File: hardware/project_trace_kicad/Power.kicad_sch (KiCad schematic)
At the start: 12 parts, among them J501 FIT0587_Male, J502 FIT0587_Female, J503 Screw_Terminal_01x04, U501 UA78M33QDCYRQ1, U502 UA78M05QDCYRQ1

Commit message: ERC Checks & Bug-Fixing
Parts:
- renumbered A501 to A401, BT501 to BT401, BT502 to BT402, C503 to C401, C504 to C402, C401 to C403, C402 to C404, J501 to J401, J502 to J402, J503 to J403, U501 to U401, U502 to U402
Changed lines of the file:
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@@
 		(dnp no)
 		(fields_autoplaced yes)
-		(property "Reference" "#PWR0501"
+		(property "Reference" "#PWR0401"
 			(at 176.53 97.79 0)
 			(hide yes)
@@
 			(project "project_trace_kicad"
 				(path "/af51f4e5-b952-4b0e-baf2-78a72fb86fcd/12a73351-c59a-4c39-a723-2f90ff2520c9"
-					(reference "#PWR0501")
+					(reference "#PWR0401")
 					(unit 1)
 				)
@@
 		(in_pos_files yes)
 		(dnp no)
-		(property "Reference" "#FLG0502"
+		(property "Reference" "#FLG0402"
 			(at 167.64 93.345 0)
 			(hide yes)
@@
 			(project "project_trace_kicad"
 				(path "/af51f4e5-b952-4b0e-baf2-78a72fb86fcd/12a73351-c59a-4c39-a723-2f90ff2520c9"
-					(reference "#FLG0502")
+					(reference "#FLG0402")
 					(unit 1)
 				)
@@
 		(dnp no)
 		(fields_autoplaced yes)
-		(property "Reference" "C504"
+		(property "Reference" "C402"
 			(at 186.3091 117.4072 0)
 			(show_name no)
@@
 			(project "project_trace_kicad"
 				(path "/af51f4e5-b952-4b0e-baf2-78a72fb86fcd/12a73351-c59a-4c39-a723-2f90ff2520c9"
-					(reference "C504")
+					(reference "C402")
 					(unit 1)
 				)
@@
 		(dnp no)
 		(fields_autoplaced yes)
-		(property "Reference" "U501"
+		(property "Reference" "U401"
 			(at 198.12 80.9455 0)
 			(show_name no)
@@
 			(project "project_trace_kicad"
 				(path "/af51f4e5-b952-4b0e-baf2-78a72fb86fcd/12a73351-c59a-4c39-a723-2f90ff2520c9"
-					(reference "U501")
+					(reference "U401")
 					(unit 1)
 				)
@@
 		(dnp yes)
 		(fields_autoplaced yes)
-		(property "Reference" "J501"
+		(property "Reference" "J401"
 			(at 122.6312 100.3878 0)
 			(show_name no)
@@
 			(project "project_trace_kicad"
 				(path "/af51f4e5-b952-4b0e-baf2-78a72fb86fcd/12a73351-c59a-4c39-a723-2f90ff2520c9"
-					(reference "J501")
+					(reference "J401")
 					(unit 1)
 				)
@@
 		(dnp yes)
 		(fields_autoplaced yes)
-		(property "Reference" "BT502"
+		(property "Reference" "BT402"
 			(at 83.439 104.8963 0)
 			(show_name no)
@@
 			(project "project_trace_kicad"
 				(path "/af51f4e5-b952-4b0e-baf2-78a72fb86fcd/12a73351-c59a-4c39-a723-2f90ff2520c9"
-					(reference "BT502")
+					(reference "BT402")
 					(unit 1)
 				)
@@
 		(dnp no)
 		(fields_autoplaced yes)
-		(property "Reference" "#PWR0401"
+		(property "Reference" "#PWR0402"
 			(at 180.34 90.17 0)
 			(hide yes)
@@
 			(project "project_trace_kicad"
 				(path "/af51f4e5-b952-4b0e-baf2-78a72fb86fcd/12a73351-c59a-4c39-a723-2f90ff2520c9"
-					(reference "#PWR0401")
+					(reference "#PWR0402")
 					(unit 1)
 				)
@@
 		(in_pos_files yes)
 		(dnp no)
-		(property "Reference" "J502"
+		(property "Reference" "J402"
 			(at 136.906 87.4917 0)
 			(show_name no)
@@
 			(project "project_trace_kicad"
 				(path "/af51f4e5-b952-4b0e-baf2-78a72fb86fcd/12a73351-c59a-4c39-a723-2f90ff2520c9"
-					(reference "J502")
+					(reference "J402")
 					(unit 1)
 				)
@@
 		(in_pos_files yes)
 		(dnp no)
-		(property "Reference" "C402"
+		(property "Reference" "C404"
 			(at 209.9309 117.4072 0)
 			(show_name no)
@@
 			(project "project_trace_kicad"
 				(path "/af51f4e5-b952-4b0e-baf2-78a72fb86fcd/12a73351-c59a-4c39-a723-2f90ff2520c9"
-					(reference "C402")
+					(reference "C404")
 					(unit 1)
 				)
@@
 		(dnp no)
 		(fields_autoplaced yes)
-		(property "Reference" "#PWR0504"
+		(property "Reference" "#PWR0405"
 			(at 215.9 90.17 0)
 			(hide yes)
@@
 			(project "project_trace_kicad"
 				(path "/af51f4e5-b952-4b0e-baf2-78a72fb86fcd/12a73351-c59a-4c39-a723-2f90ff2520c9"
-					(reference "#PWR0504")
+					(reference "#PWR0405")
 					(unit 1)
 				)
@@
 		(dnp yes)
 		(fields_autoplaced yes)
-		(property "Reference" "BT501"
+		(property "Reference" "BT401"
 			(at 83.439 94.7363 0)
 			(show_name no)
@@
 			(project "project_trace_kicad"
 				(path "/af51f4e5-b952-4b0e-baf2-78a72fb86fcd/12a73351-c59a-4c39-a723-2f90ff2520c9"
-					(reference "BT501")
+					(reference "BT401")
 					(unit 1)
 				)
@@
 		(in_pos_files yes)
 		(dnp no)
-		(property "Reference" "J503"
+		(property "Reference" "J403"
 			(at 150.368 91.44 0)
 			(show_name no)
@@
 			(project "project_trace_kicad"
 				(path "/af51f4e5-b952-4b0e-baf2-78a72fb86fcd/12a73351-c59a-4c39-a723-2f90ff2520c9"
-					(reference "J503")
+					(reference "J403")
 					(unit 1)
 				)
@@
 		(dnp no)
 		(fields_autoplaced yes)
-		(property "Reference" "U502"
+		(property "Reference" "U402"
 			(at 198.12 107.6155 0)
 			(show_name no)
@@
 			(project "project_trace_kicad"
 				(path "/af51f4e5-b952-4b0e-baf2-78a72fb86fcd/12a73351-c59a-4c39-a723-2f90ff2520c9"
-					(reference "U502")
+					(reference "U402")
 					(unit 1)
 				)
@@
 		(dnp yes)
 		(fields_autoplaced yes)
-		(property "Reference" "A501"
+		(property "Reference" "A401"
 			(at 105.41 92.5025 0)
 			(show_name no)
@@
 			(project "project_trace_kicad"
 				(path "/af51f4e5-b952-4b0e-baf2-78a72fb86fcd/12a73351-c59a-4c39-a723-2f90ff2520c9"
-					(reference "A501")
+					(reference "A401")
 					(unit 1)
 				)
@@
 		(dnp no)
 		(fields_autoplaced yes)
-		(property "Reference" "#PWR0505"
+		(property "Reference" "#PWR0406"
 			(at 215.9 116.84 0)
 			(hide yes)
@@
 			(project "project_trace_kicad"
 				(path "/af51f4e5-b952-4b0e-baf2-78a72fb86fcd/12a73351-c59a-4c39-a723-2f90ff2520c9"
-					(reference "#PWR0505")
+					(reference "#PWR0406")
 					(unit 1)
 				)
@@
 		(dnp no)
 		(fields_autoplaced yes)
-		(property "Reference" "C503"
+		(property "Reference" "C401"
 			(at 186.3091 90.7372 0)
 			(show_name no)
@@
 			(project "project_trace_kicad"
 				(path "/af51f4e5-b952-4b0e-baf2-78a72fb86fcd/12a73351-c59a-4c39-a723-2f90ff2520c9"
-					(reference "C503")
+					(reference "C401")
 					(unit 1)
 				)
@@
 		(in_pos_files yes)
 		(dnp no)
-		(property "Reference" "C401"
+		(property "Reference" "C403"
 			(at 209.9309 90.7372 0)
 			(show_name no)
@@
 			(project "project_trace_kicad"
 				(path "/af51f4e5-b952-4b0e-baf2-78a72fb86fcd/12a73351-c59a-4c39-a723-2f90ff2520c9"
-					(reference "C401")
+					(reference "C403")
 					(unit 1)
 				)
@@
 		(dnp no)
 		(fields_autoplaced yes)
-		(property "Reference" "#PWR0503"
+		(property "Reference" "#PWR0404"
 			(at 198.12 132.08 0)
 			(hide yes)
@@
 			(project "project_trace_kicad"
 				(path "/af51f4e5-b952-4b0e-baf2-78a72fb86fcd/12a73351-c59a-4c39-a723-2f90ff2520c9"
-					(reference "#PWR0503")
+					(reference "#PWR0404")
 					(unit 1)
 				)
@@
 		(dnp no)
 		(fields_autoplaced yes)
-		(property "Reference" "#FLG0501"
+		(property "Reference" "#FLG0401"
 			(at 167.64 84.455 0)
 			(hide yes)
@@
 			(project "project_trace_kicad"
 				(path "/af51f4e5-b952-4b0e-baf2-78a72fb86fcd/12a73351-c59a-4c39-a723-2f90ff2520c9"
-					(reference "#FLG0501")
+					(reference "#FLG0401")
 					(unit 1)
 				)
@@
 		(dnp no)
 		(fields_autoplaced yes)
-		(property "Reference" "#PWR0502"
+		(property "Reference" "#PWR0403"
 			(at 198.12 105.41 0)
 			(hide yes)
@@
 			(project "project_trace_kicad"
 				(path "/af51f4e5-b952-4b0e-baf2-78a72fb86fcd/12a73351-c59a-4c39-a723-2f90ff2520c9"
-					(reference "#PWR0502")
-					(unit 1)
-				)
+					(reference "#PWR0403")
+					(unit 1)
+				)

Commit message: Partnumbers and BOM updated
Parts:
- A401, BT401, BT402: DigikeyPN N/A -> (none); now left out of the parts list
- J401: DigikeyPN 1738-1437-ND -> (none); MouserPN 426-FIT0587 -> (none); now left out of the parts list
- J402: DigikeyPN 1738-1437-ND -> (none); MouserPN 426-FIT0587 -> (none)
- J403: MouserPN 710-691210910004 -> (none)
- U401: MouserPN 595-UA78M33CKVURG3 -> (none)
- U402: MouserPN 595-UA78M05CKVURG3 -> (none)
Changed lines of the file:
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@@
-			)
-		)
-		(property "MouserPN" "595-UA78M33CKVURG3"
-			(at 198.12 87.63 0)
-			(hide yes)
-			(show_name no)
-			(do_not_autoplace no)
-			(effects
-				(font
-					(size 1.27 1.27)
-				)
 			)
 		)
@@
 		(body_style 1)
 		(exclude_from_sim no)
-		(in_bom yes)
+		(in_bom no)
 		(on_board no)
 		(in_pos_files yes)
@@
 			)
 		)
-		(property "MouserPN" "426-FIT0587"
-			(at 121.92 100.33 0)
-			(hide yes)
-			(show_name no)
-			(do_not_autoplace no)
-			(effects
-				(font
-					(size 1.27 1.27)
-				)
-			)
-		)
-		(property "DigikeyPN" "1738-1437-ND"
-			(at 121.92 100.33 0)
-			(hide yes)
-			(show_name no)
-			(do_not_autoplace no)
-			(effects
-				(font
-					(size 1.27 1.27)
-				)
-			)
-		)
 		(pin "1"
 		)
@@
 		(body_style 1)
 		(exclude_from_sim no)
-		(in_bom yes)
+		(in_bom no)
 		(on_board no)
 		(in_pos_files yes)
@@
 			)
 		)
-		(property "DigikeyPN" "N/A"
-			(at 86.36 107.95 0)
-			(hide yes)
-			(show_name no)
-			(do_not_autoplace no)
-			(effects
-				(font
-					(size 1.27 1.27)
-				)
-			)
-		)
 		(pin "1"
 		)
@@
 		(exclude_from_sim no)
 		(in_bom no)
-		(on_board yes)
+		(on_board no)
 		(in_pos_files yes)
 		(dnp no)
@@
 		)
 		(property "Description" "Generic connector, single row, 01x02, script generated"
-			(at 144.78 87.63 0)
-			(hide yes)
-			(show_name no)
-			(do_not_autoplace no)
-			(effects
-				(font
-					(size 1.27 1.27)
-				)
-			)
-		)
-		(property "MouserPN" "426-FIT0587"
-			(at 144.78 87.63 0)
-			(hide yes)
-			(show_name no)
-			(do_not_autoplace no)
-			(effects
-				(font
-					(size 1.27 1.27)
-				)
-			)
-		)
-		(property "DigikeyPN" "1738-1437-ND"
 			(at 144.78 87.63 0)
 			(hide yes)
@@
 		(body_style 1)
 		(exclude_from_sim no)
-		(in_bom yes)
+		(in_bom no)
 		(on_board no)
 		(in_pos_files yes)
@@
 			)
 		)
-		(property "DigikeyPN" "N/A"
-			(at 86.36 97.79 0)
-			(hide yes)
-			(show_name no)
-			(do_not_autoplace no)
-			(effects
-				(font
-					(size 1.27 1.27)
-				)
-			)
-		)
 		(pin "1"
 		)
@@
 		)
 		(property "Description" "Generic screw terminal, single row, 01x04, script generated (kicad-library-utils/schlib/autogen/connector/)"
-			(at 152.4 90.17 0)
-			(hide yes)
-			(show_name no)
-			(do_not_autoplace no)
-			(effects
-				(font
-					(size 1.27 1.27)
-				)
-			)
-		)
-		(property "MouserPN" "710-691210910004"
 			(at 152.4 90.17 0)
 			(hide yes)
@@
 			)
 		)
-		(property "MouserPN" "595-UA78M05CKVURG3"
-			(at 198.12 114.3 0)
-			(hide yes)
-			(show_name no)
-			(do_not_autoplace no)
-			(effects
-				(font
-					(size 1.27 1.27)
-				)
-			)
-		)
 		(property "DigikeyPN" "296-19755-1-ND"
 			(at 198.12 114.3 0)
@@
 		(body_style 1)
 		(exclude_from_sim no)
-		(in_bom yes)
+		(in_bom no)
 		(on_board no)
 		(in_pos_files yes)
@@
 			(at 105.41 101.6 0)
 			(hide yes)
-			(show_name no)
-			(do_not_autoplace no)
-			(effects
-				(font
-					(size 1.27 1.27)
-				)
-			)
-		)
-		(property "DigikeyPN" "N/A"
-			(at 105.41 101.6 0)
-			(hide yes)

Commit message: Improvements to Power layout and Silkscreen
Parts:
- removed U402: UA78M05QDCYRQ1, Package_TO_SOT_SMD:SOT-223-3_TabPin2, symbol Regulator_Linear:UA78M05QDCYRQ1
- added U402: AMS1117-5.0, Package_TO_SOT_SMD:SOT-223-3_TabPin2, symbol Regulator_Linear:AMS1117-5.0
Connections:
- net +5V: now also U402.2 (VO)
- net GND: now also U402.1 (GND)
- net VBAT: now also U402.3 (VI)
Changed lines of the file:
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@@
+			)
+		)
+		(property "DIgikeyPN" ""
+			(at 189.23 119.38 0)
+			(hide yes)
+			(show_name no)
+			(do_not_autoplace no)
+			(effects
+				(font
+					(size 1.27 1.27)
+				)
 			)
 		)
@@
 			)
 		)
+		(property "DIgikeyPN" ""
+			(at 198.12 87.63 0)
+			(hide yes)
+			(show_name no)
+			(do_not_autoplace no)
+			(effects
+				(font
+					(size 1.27 1.27)
+				)
+			)
+		)
 		(pin "3"
 		)
@@
 				(path "/af51f4e5-b952-4b0e-baf2-78a72fb86fcd/12a73351-c59a-4c39-a723-2f90ff2520c9"
 					(reference "U401")
+					(unit 1)
+				)
+			)
+		)
+	)
+	(symbol
+		(lib_id "Regulator_Linear:AMS1117-5.0")
+		(at 198.12 114.3 0)
+		(unit 1)
+		(body_style 1)
+		(exclude_from_sim no)
+		(in_bom yes)
+		(on_board yes)
+		(in_pos_files yes)
+		(dnp no)
+		(fields_autoplaced yes)
+		(property "Reference" "U402"
+			(at 198.12 108.6356 0)
+			(show_name no)
+			(do_not_autoplace no)
+			(effects
+				(font
+					(size 1.27 1.27)
+				)
+			)
+		)
+		(property "Value" "AMS1117-5.0"
+			(at 198.12 110.8032 0)
+			(show_name no)
+			(do_not_autoplace no)
+			(effects
+				(font
+					(size 1.27 1.27)
+				)
+			)
+		)
+		(property "Footprint" "Package_TO_SOT_SMD:SOT-223-3_TabPin2"
+			(at 198.12 109.22 0)
+			(hide yes)
+			(show_name no)
+			(do_not_autoplace no)
+			(effects
+				(font
+					(size 1.27 1.27)
+				)
+			)
+		)
+		(property "Datasheet" "http://www.advanced-monolithic.com/pdf/ds1117.pdf"
+			(at 200.66 120.65 0)
+			(hide yes)
+			(show_name no)
+			(do_not_autoplace no)
+			(effects
+				(font
+					(size 1.27 1.27)
+				)
+			)
+		)
+		(property "Description" "1A Low Dropout regulator, positive, 5.0V fixed output, SOT-223"
+			(at 198.12 114.3 0)
+			(hide yes)
+			(show_name no)
+			(do_not_autoplace no)
+			(effects
+				(font
+					(size 1.27 1.27)
+				)
+			)
+		)
+		(property "DIgikeyPN" ""
+			(at 198.12 114.3 0)
+			(hide yes)
+			(show_name no)
+			(do_not_autoplace no)
+			(effects
+				(font
+					(size 1.27 1.27)
+				)
+			)
+		)
+		(property "DigikeyPN" "5272-AMS1117-5.0CT-ND"
+			(at 198.12 114.3 0)
+			(hide yes)
+			(show_name no)
+			(do_not_autoplace no)
+			(effects
+				(font
+					(size 1.27 1.27)
+				)
+			)
+		)
+		(pin "1"
+		)
+		(pin "2"
+		)
+		(pin "3"
+		)
+		(instances
+			(project "project_trace_kicad"
+				(path "/af51f4e5-b952-4b0e-baf2-78a72fb86fcd/12a73351-c59a-4c39-a723-2f90ff2520c9"
+					(reference "U402")
 					(unit 1)
 				)
@@
 			)
 		)
+		(property "DIgikeyPN" ""
+			(at 121.92 100.33 0)
+			(hide yes)
+			(show_name no)
+			(do_not_autoplace no)
+			(effects
+				(font
+					(size 1.27 1.27)
+				)
+			)
+		)
 		(pin "1"
 		)
@@
 			)
 		)
+		(property "DIgikeyPN" ""
+			(at 86.36 107.95 0)
+			(hide yes)
+			(show_name no)
+			(do_not_autoplace no)
+			(effects
+				(font
+					(size 1.27 1.27)
+				)
+			)
+		)
 		(pin "1"
 		)
@@
 			)
 		)
+		(property "DIgikeyPN" ""
+			(at 144.78 87.63 0)
+			(hide yes)
+			(show_name no)
+			(do_not_autoplace no)
+			(effects
+				(font
+					(size 1.27 1.27)
+				)
+			)
+		)
 		(pin "1"
 		)
@@
 			)
 		)
+		(property "DIgikeyPN" ""
+			(at 207.01 119.38 0)
+			(hide yes)
+			(show_name no)
+			(do_not_autoplace no)
+			(effects
+				(font
+					(size 1.27 1.27)
+				)
+			)
+		)
 		(pin "1"
 		)
@@
 			)
 		)
+		(property "DIgikeyPN" ""
+			(at 86.36 97.79 0)
+			(hide yes)
+			(show_name no)
+			(do_not_autoplace no)
+			(effects
+				(font
+					(size 1.27 1.27)
+				)
+			)
+		)
 		(pin "1"
 		)
@@
 			)
 		)
+		(property "DIgikeyPN" ""
+			(at 152.4 90.17 0)
+			(hide yes)
+			(show_name no)
+			(do_not_autoplace no)
+			(effects
+				(font
+					(size 1.27 1.27)
+				)
+			)
+		)
 		(pin "4"
 		)
@@
 				(path "/af51f4e5-b952-4b0e-baf2-78a72fb86fcd/12a73351-c59a-4c39-a723-2f90ff2520c9"
 					(reference "J403")
-					(unit 1)
-				)
-			)
-		)
-	)
-	(symbol
-		(lib_id "Regulator_Linear:UA78M05QDCYRQ1")
-		(at 198.12 114.3 0)
-		(unit 1)
-		(body_style 1)
-		(exclude_from_sim no)
-		(in_bom yes)
-		(on_board yes)
-		(in_pos_files yes)
-		(dnp no)
-		(fields_autoplaced yes)
-		(property "Reference" "U402"
-			(at 198.12 107.6155 0)
-			(show_name no)
-			(do_not_autoplace no)
-			(effects
-				(font
-					(size 1.27 1.27)
-				)
-			)
-		)
-		(property "Value" "UA78M05QDCYRQ1"
-			(at 198.12 110.0398 0)
-			(show_name no)
-			(do_not_autoplace no)
-			(effects
-				(font
-					(size 1.27 1.27)
-				)
-			)
-		)
-		(property "Footprint" "Package_TO_SOT_SMD:SOT-223-3_TabPin2"
-			(at 198.755 118.11 0)
-			(hide yes)
-			(show_name no)
-			(do_not_autoplace no)
-			(effects
-				(font
-					(size 1.27 1.27)
-					(italic yes)
-				)
-				(justify left)
-			)
-		)
-		(property "Datasheet" "https://www.ti.com/lit/gpn/UA78M-Q1"
-			(at 198.12 115.57 0)
-			(hide yes)
-			(show_name no)
-			(do_not_autoplace no)
-			(effects
-				(font
-					(size 1.27 1.27)
-				)
-			)
-		)
-		(property "Description" "Positive 500mA 25V Linear Regulator, Fixed Output 5V, SOT-223"
-			(at 198.12 114.3 0)
-			(hide yes)
-			(show_name no)
-			(do_not_autoplace no)
-			(effects
-				(font
-					(size 1.27 1.27)
-				)
-			)
-		)
-		(property "DigikeyPN" "296-19755-1-ND"
-			(at 198.12 114.3 0)
-			(hide yes)
-			(show_name no)
-			(do_not_autoplace no)
-			(effects
-				(font
-					(size 1.27 1.27)
-				)
-			)
-		)
-		(pin "3"
-		)
-		(pin "2"
-		)
-		(pin "1"
-		)
-		(instances
-			(project "project_trace_kicad"
-				(path "/af51f4e5-b952-4b0e-baf2-78a72fb86fcd/12a73351-c59a-4c39-a723-2f90ff2520c9"
-					(reference "U402")
 					(unit 1)
 				)
@@
 			)
 		)
+		(property "DIgikeyPN" ""
+			(at 105.41 101.6 0)
+			(hide yes)
+			(show_name no)
+			(do_not_autoplace no)
+			(effects
+				(font
+					(size 1.27 1.27)
+				)
+			)
+		)
 		(pin "2"
 		)
@@
 			)
 		)
+		(property "DIgikeyPN" ""
+			(at 189.23 92.71 0)
+			(hide yes)
+			(show_name no)
+			(do_not_autoplace no)
+			(effects
+				(font
+					(size 1.27 1.27)
+				)
+			)
+		)
 		(pin "1"
 		)
@@
 			(at 207.01 92.71 0)
 			(hide yes)
+			(show_name no)
+			(do_not_autoplace no)
+			(effects
+				(font
+					(size 1.27 1.27)
+				)
+			)
+		)
+		(property "DIgikeyPN" ""
+			(at 207.01 92.71 0)
+			(hide yes)

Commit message: Fix wrong partno, add debug LED
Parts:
- U401: DigikeyPN 296-21208-1-ND -> 296-13424-1-ND
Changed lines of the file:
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@@
 			)
 		)
-		(property "DigikeyPN" "296-21208-1-ND"
+		(property "DigikeyPN" "296-13424-1-ND"
 			(at 198.12 87.63 0)
 			(hide yes)

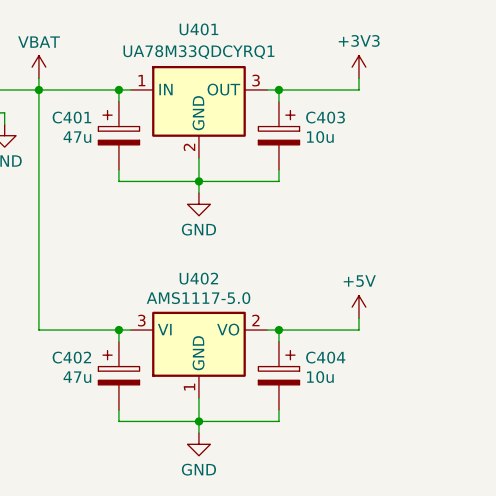
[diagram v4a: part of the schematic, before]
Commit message: Review 1 issues adressed
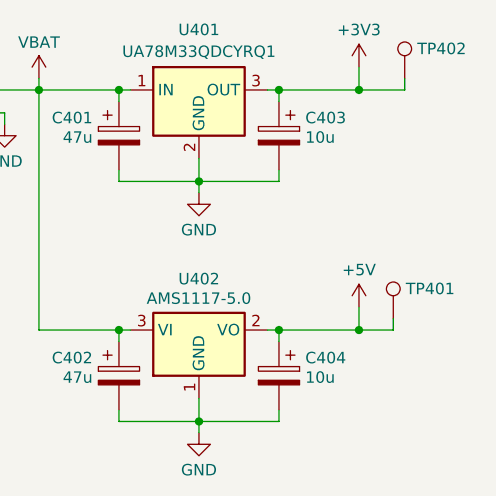
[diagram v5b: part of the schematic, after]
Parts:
- added TP401, TP402: TestPoint, TestPoint:TestPoint_Pad_1.5x1.5mm, symbol Connector:TestPoint
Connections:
- net +3V3: now also TP402.1
- net +5V: now also TP401.1

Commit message: Address items of internal review
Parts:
- A401, BT401, BT402, J401, J402: DigikeyPN (none) -> N/A
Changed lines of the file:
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@@
 	(title_block
 		(title "Multilloscope - Power")
-		(date "2026-04-06")
-		(rev "1")
+		(date "2026-04-19")
+		(rev "2")
 		(comment 1 "Laurits K. Hillemann")
 		(comment 2 "Alexander N. Olsen")
@@
 			)
 		)
+		(property "DigikeyPN" "N/A"
+			(at 121.92 100.33 0)
+			(hide yes)
+			(show_name no)
+			(do_not_autoplace no)
+			(effects
+				(font
+					(size 1.27 1.27)
+				)
+			)
+		)
 		(pin "1"
 		)
@@
 			)
 		)
+		(property "DigikeyPN" "N/A"
+			(at 86.36 107.95 0)
+			(hide yes)
+			(show_name no)
+			(do_not_autoplace no)
+			(effects
+				(font
+					(size 1.27 1.27)
+				)
+			)
+		)
 		(pin "1"
 		)
@@
 			)
 		)
+		(property "DigikeyPN" "N/A"
+			(at 144.78 87.63 0)
+			(hide yes)
+			(show_name no)
+			(do_not_autoplace no)
+			(effects
+				(font
+					(size 1.27 1.27)
+				)
+			)
+		)
 		(pin "1"
 		)
@@
 			)
 		)
+		(property "DigikeyPN" "N/A"
+			(at 86.36 97.79 0)
+			(hide yes)
+			(show_name no)
+			(do_not_autoplace no)
+			(effects
+				(font
+					(size 1.27 1.27)
+				)
+			)
+		)
 		(pin "1"
 		)
@@
 			(at 105.41 101.6 0)
 			(hide yes)
+			(show_name no)
+			(do_not_autoplace no)
+			(effects
+				(font
+					(size 1.27 1.27)
+				)
+			)
+		)
+		(property "DigikeyPN" "N/A"
+			(at 105.41 101.6 0)
+			(hide yes)
